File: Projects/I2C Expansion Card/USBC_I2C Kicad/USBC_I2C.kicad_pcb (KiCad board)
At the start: 2 copper layers, 26 x 27.9 mm, 33 parts, among them J1 2.54mm Pitch Header, J2 2.54mm Pitch Header, J3 2.54mm Pitch Header, Q1 DMC2053UVT, SW1 SW_DIP_x04, U1 MCP2221AxSL, U2 LTC4412xS6

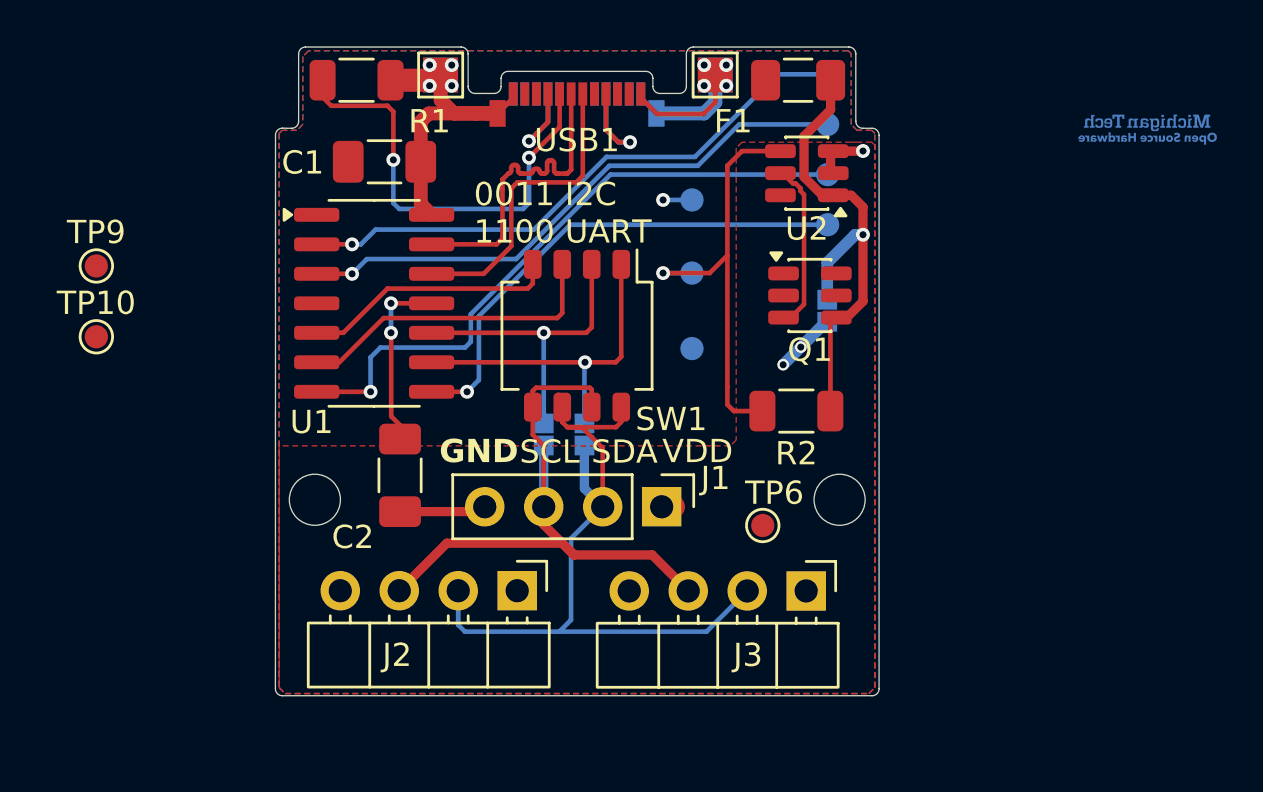
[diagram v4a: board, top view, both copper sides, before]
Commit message: Finished improving I2C/UART Card
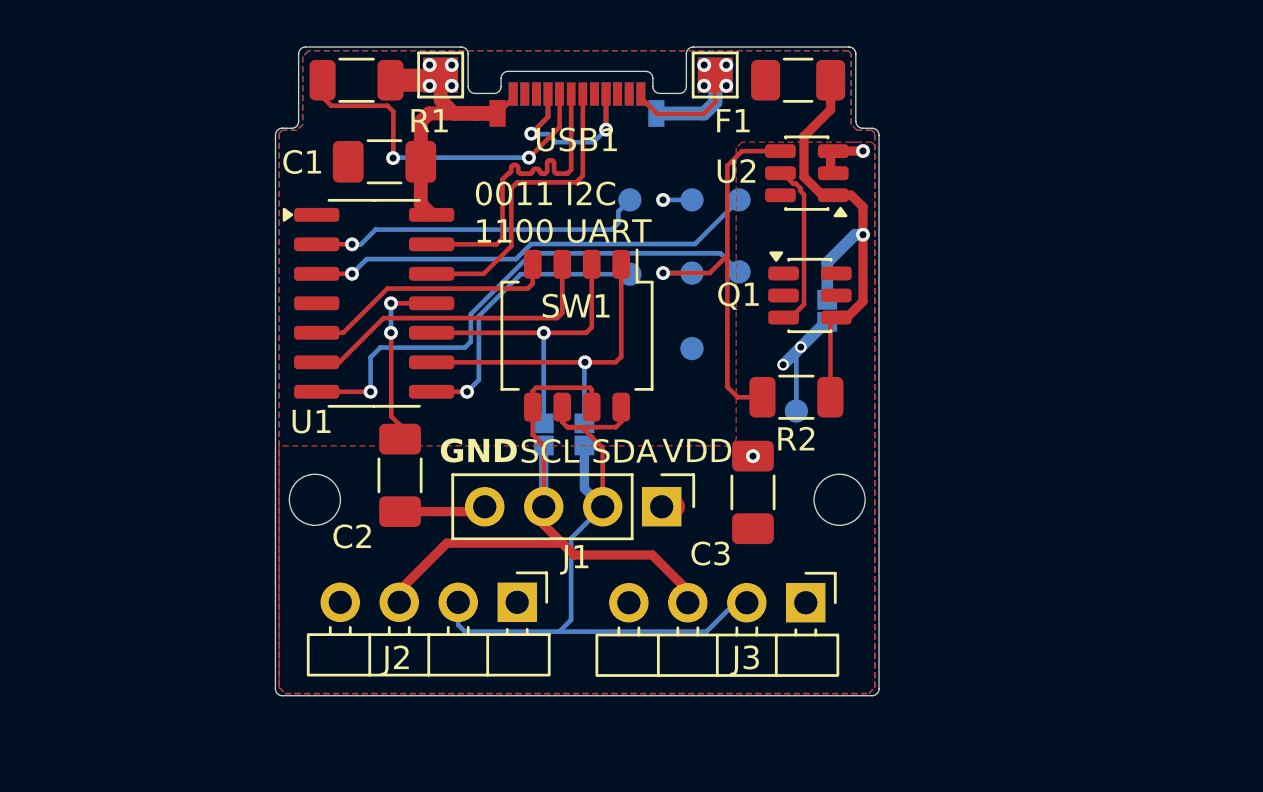
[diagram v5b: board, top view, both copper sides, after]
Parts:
- removed TP10: D-, TestPoint:TestPoint_Pad_D1.0mm
- removed TP9: D+, TestPoint:TestPoint_Pad_D1.0mm
- added C3: 10uF, Capacitor_SMD:C_1206_3216Metric_Pad1.33x1.80mm_HandSolder, F.Cu at (104.1, 76.3)
- G***: moved to F.Cu
- TP6: moved to B.Cu
- moved G*** 31.3 mm to (90.4, 64.7), turned to 0 degrees
- moved TP1 10.1 mm to (98.8, 63.7)
- moved TP4 8.78 mm to (98.8, 66.9)
- moved TP3 5.67 mm to (103.5, 66.8)
- moved TP6 5.14 mm to (106.0, 72.8), turned to 180 degrees
- moved TP2 5.01 mm to (103.5, 63.7)
- moved J3 1.89 mm to (105.1, 81.9)
- moved R2 0.60 mm to (106.0, 72.2)
- moved J2 0.50 mm to (93.9, 81.0)
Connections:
- SW1 pad 5: /SCL/UTx -> /Out1
- SW1 pad 6: /SDA/URx -> /Out0
- SW1 pad 7: /SCL/UTx -> /Out1
- SW1 pad 8: /SDA/URx -> /Out0
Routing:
- net Net-(U1-GP0): track 25.0 -> 14.6 mm
- net Net-(U1-GP3): track 21.6 -> 12.3 mm
- net Net-(U1-GP1): track 24.7 -> 19.5 mm
- net Net-(U1-GP2): track 27.4 -> 22.6 mm
- net Net-(USB1-CC): track 19.3 -> 15.2 mm
- net /Vo: track 3.30 -> 6.13 mm
- net Net-(U2-STAT): track 18.7 -> 18.0 mm
- net GND: vias 9 -> 10
